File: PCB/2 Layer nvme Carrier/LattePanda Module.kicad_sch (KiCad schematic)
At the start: 31 parts, among them J1 Conn_01x03_Pin, J81 Conn_01x02_Pin, U80 W25Q128JVSIQ

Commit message: Rework started with PCIe
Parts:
- removed C86, C89: 22uF/6.3V, A_HDJ_Library:C_0402_1005Metric, symbol Device:C
- removed C87, C90: 0.1uF/16V, A_HDJ_Library:C_0402_1005Metric, symbol Device:C
- removed D78: D_Schottky, Diode_SMD:D_SOD-923, symbol Device:D_Schottky
- removed Q78: ~, Package_SO:TSSOP-20_4.4x6.5mm_P0.65mm, symbol User:9DBL411BGLFT
- removed Q79: ~, Package_SO:TSSOP-48_6.1x12.5mm_P0.5mm, symbol User:PI6C20800AE
- removed R80: 0R, A_HDJ_Library:R_0402_1005Metric, symbol Device:R
- removed R81, R82, R83, R84, R85: 15R/1%, A_HDJ_Library:R_0402_1005Metric, symbol Device:R
- removed R86: 120K/1%, A_HDJ_Library:R_0402_1005Metric, symbol Device:R
- removed R87, R88, R89, R90: 1K/1%, A_HDJ_Library:R_0402_1005Metric, symbol Device:R
- removed U80: W25Q128JVSIQ, Package_SO:SOIC-8_5.23x5.23mm_P1.27mm, symbol Memory_Flash:W25Q128JVS
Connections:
- net SPI-IO3: now reaches A1.153 (SPI_IO3)
- net SPI_CLK: now reaches A1.155 (SPI_CLK)
- net SPI-IO0: now reaches A1.159 (SPI_MOSI/SPI_IO0)
- net SPI-IO2: now reaches A1.161 (SPI_IO2)
- net SPI-IO1: now reaches A1.163 (SPI_MISO/SPI_IO1)
- net SPI-CS: now reaches A1.165 (~{SPI_CS})
- net REFCLK2+: now reaches A1.97 (REFCLK2+)
- net REFCLK2-: now reaches A1.99 (REFCLK2-)
- net SUSCLK_WIFI: no longer names the net of A1.131 (SUSCLK)
- no-connect marks 94 -> 95
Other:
- note added: "USB2_P6 is reserved for TypeC PD Controller"
- note removed: "USB2_P6 is reserved for TypeC PD Controller DO NOT use it as a normal USB"
- moved on the sheet: R78, R79

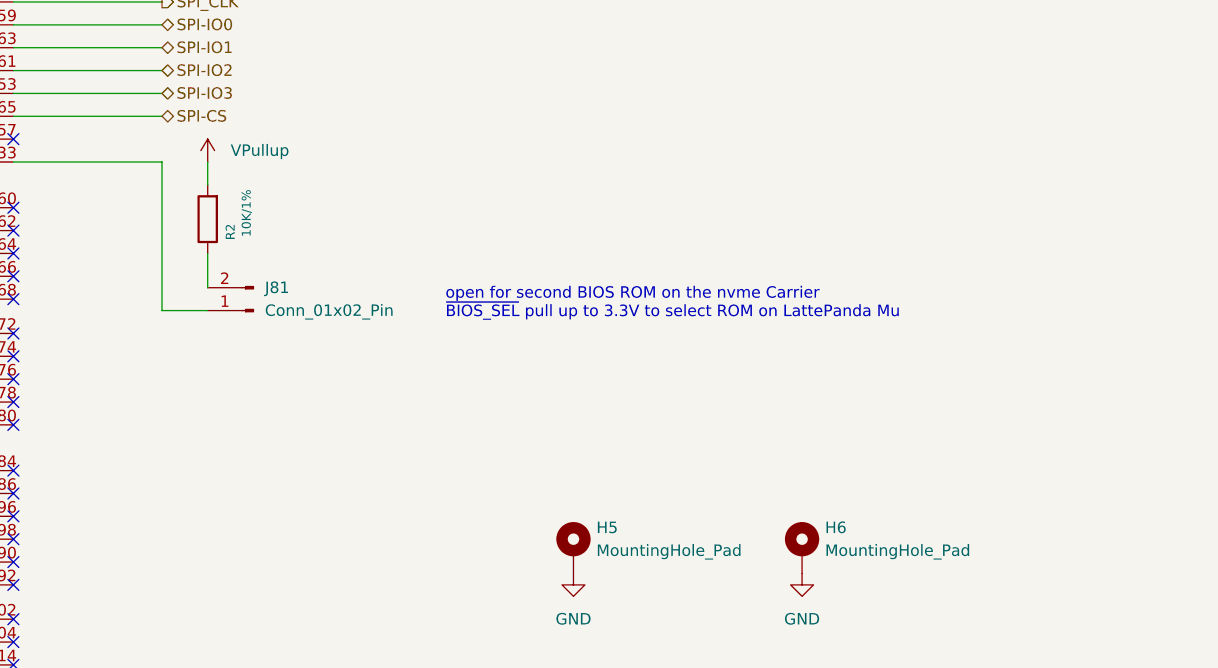
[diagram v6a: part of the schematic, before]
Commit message: PCIe and CLK Buffenr Lines
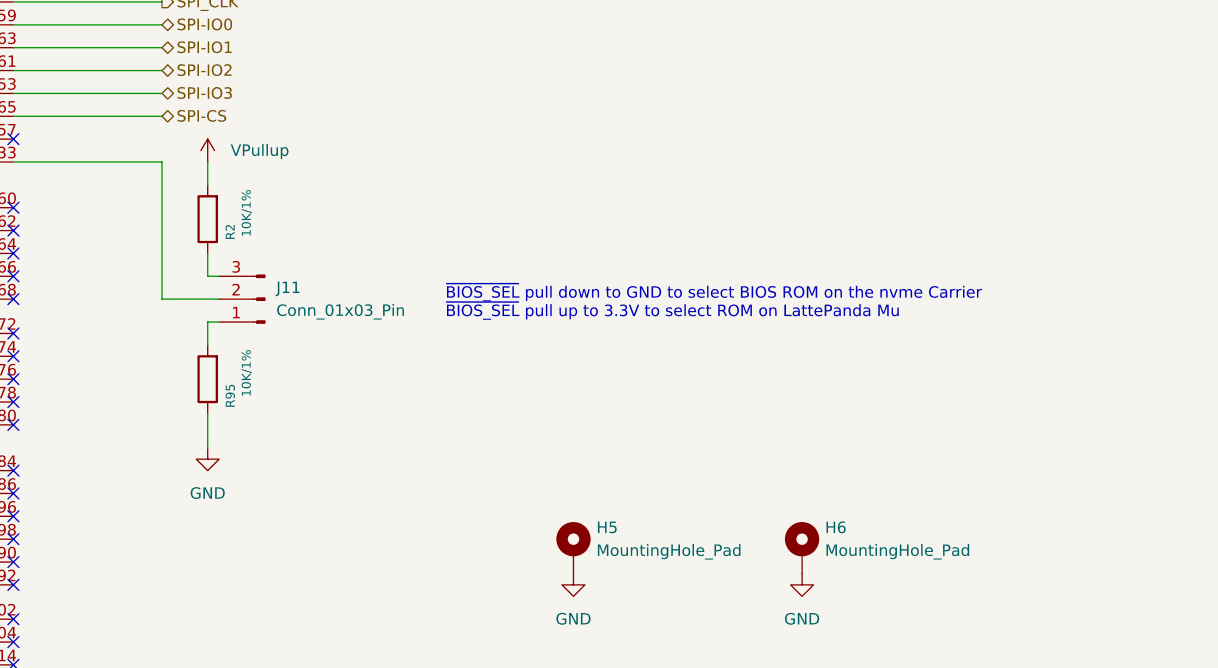
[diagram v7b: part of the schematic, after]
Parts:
- removed J81: Conn_01x02_Pin, Connector_PinHeader_2.54mm:PinHeader_1x02_P2.54mm_Vertical, symbol Connector:Conn_01x02_Pin
- added J11: Conn_01x03_Pin, Connector_PinHeader_2.54mm:PinHeader_1x03_P2.54mm_Vertical, symbol Connector:Conn_01x03_Pin
- added R95: 10K/1%, A_HDJ_Library:R_0402_1005Metric, symbol Device:R
- J1: footprint A_HDJ_Library:PinHeader_1x03_P2.54mm_Vertical -> Connector_PinHeader_2.54mm:PinHeader_1x03_P2.54mm_Vertical
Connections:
- net GND: now also R95.1
- net at A1.133 (~{BIOS_SEL}): now also J11.2 (Pin_2)
- net at R2.1: now also J11.3 (Pin_3)
- new net: J11.1 (Pin_1), R95.2
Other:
- note added: "~{BIOS_SEL} pull down to GND to select BIOS ROM on the nvme Carrier ~{BIOS_SEL} pull up to 3.3V to select ROM on LattePanda Mu"
- note removed: "open for second BIOS ROM on the nvme Carrier ~{BIOS_SEL} pull up to 3.3V to select ROM on LattePanda Mu"
